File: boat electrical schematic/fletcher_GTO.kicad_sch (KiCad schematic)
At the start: 21 parts, among them J1 IGNITION PROBE, K1 FRC2C, K2 FRC2C, K3 DIPxx-1Cxx-51x, K4 DIPxx-1Cxx-51x, M1 PUMP, M2 TRIM, SW1 LIGHT, SW2 HORN, SW3 PUMP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

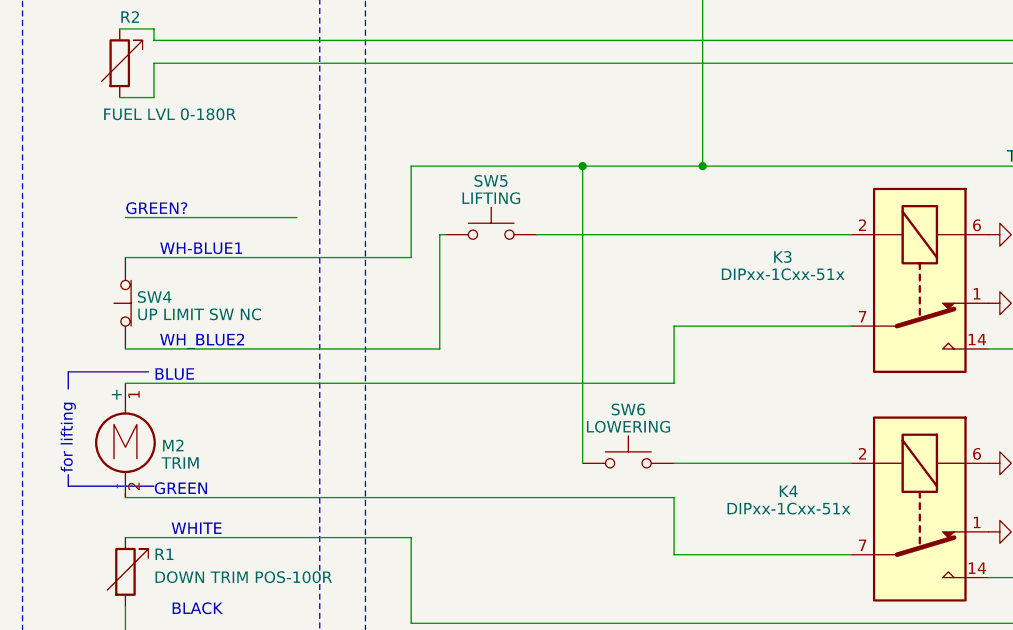
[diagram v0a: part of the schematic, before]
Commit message: add working low fuel alert, add display re-init
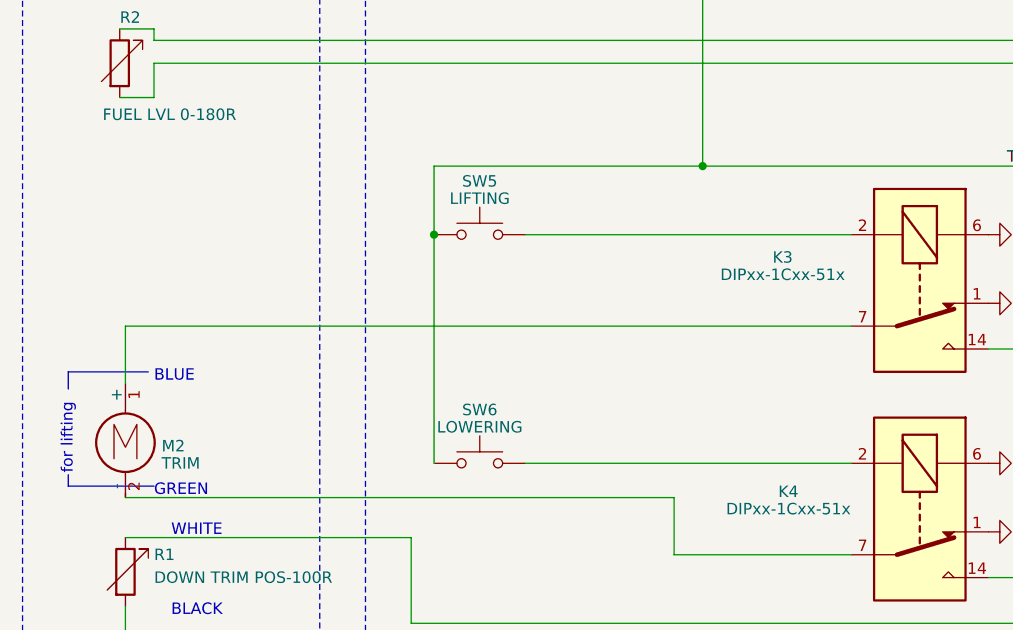
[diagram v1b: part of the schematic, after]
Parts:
- removed SW4: UP LIMIT SW NC, symbol Switch:SW_Push_Open
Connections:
- net TRIM: now also SW5.1
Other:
- note removed: "GREEN?"
- note removed: "WH-BLUE1"
- note removed: "WH_BLUE2"
- moved on the sheet: SW5, SW6

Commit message: add GDT
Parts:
- removed R1: DOWN TRIM POS-100R, symbol Device:R_Variable
- J1: value IGNITION PROBE -> CZUJNIK ZAPŁONU
- K1, K2: Field4 YL -> ŻÓŁTY; Field5 YL -> ŻÓŁTY; Field6 BLUE -> NIEBIESKI; Field7 BLACK -> CZARNY; Field8 RED -> CZERWONY
- LA1: value LIGHT -> ŚWIATŁA
- M1: value PUMP -> POMPA
- R2: value FUEL LVL 0-180R -> PŁYWAK PALIWA 0-180R
- SW1: value LIGHT -> ŚWIATŁA- włącznik
- SW2: value HORN -> KLAKSON- włącznik
- SW3: value PUMP -> POMPA- włącznik
- SW5: value LIFTING -> PODNOSZENIE
- SW6: value LOWERING -> OPUSZCZANIE
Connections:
- net HORN renamed KLAKSON
- net LIGHT renamed ŚWIATŁA
- net PUMP renamed POMPA
- net TACHO renamed KOMPUTER
- net TRIM renamed TRYM
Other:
- note added: "BEZPIECZNIK(OD LEWEJ) 1. POMPA 5A 2. KLAKSON 10A 3. SONAR 1A 4. ZAPALNICZKA 4A 5. KOMPUTER 1A 6. OŚWIETLENIE 1A"
- note added: "BRĄZOWY"
- note added: "DZIÓB"
- note added: "NIEBIESKI"
- note added: "NIEBIESKI-MASA"
- note added: "RUFA"
- note added: "ZIELONY"
- note added: "polaryzacja dla podnoszenia"
- note added: "ŻÓŁTO-ZIELONY"
- note removed: "BLACK"
- note removed: "BLUE"
- note removed: "BOW"
- note removed: "BROWN"
- note removed: "GREEN"
- note removed: "STERN"
- note removed: "WHITE"
- note removed: "for lifting"
- moved on the sheet: BT1, CS1, F1, J1, K1, K2, K3, K4, LA1, LS1, M1, R2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

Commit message: dont know
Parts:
- added F2: 4A, symbol Device:Fuse
- added J2: ZAPALNICZKA, symbol Connector_Generic:Conn_01x02
- added R1: BOCZNIK- 50mR, symbol Device:R
- added U1: OBCIĄZENIE TRYMU, symbol fletcherLib:DIFF
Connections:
- net +12V: now also F2.2
- net GND: now also J2.2 (Pin_2), U1.2 (GND)
- net TRYM: now also R1.1, U1.3 (DIFF); no longer F1.12 (OUT6)
- new net: F2.1, R1.2, U1.1 (Vcc)
- new net ZAPALNICZKA: F1.12 (OUT6), J2.1 (Pin_1)
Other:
- note added: "BEZPIECZNIK(OD LEWEJ) 1. POMPA 5A 2. KLAKSON 10A 3. SONAR 1A 4. ZAPALNICZKA 4A 5. KOMPUTER 1A 6. OŚWIETLENIE 1A BEZPIECZNIK TRYMU: 4A"
- note removed: "BEZPIECZNIK(OD LEWEJ) 1. POMPA 5A 2. KLAKSON 10A 3. SONAR 1A 4. ZAPALNICZKA 4A 5. KOMPUTER 1A 6. OŚWIETLENIE 1A"
- note removed: "NIEBIESKI"
- note removed: "ZIELONY"
- title: (none) -> Schemat elektryczny Fletcher GTO
- moved on the sheet: K3, K4, SW5
